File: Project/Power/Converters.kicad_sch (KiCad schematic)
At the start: 36 parts, among them J16 5V_2A, J17 5V_6A, U15 TPS560200, U16 MIC5219-3.3YM5, U17 TPS562200, U18 TPS54627

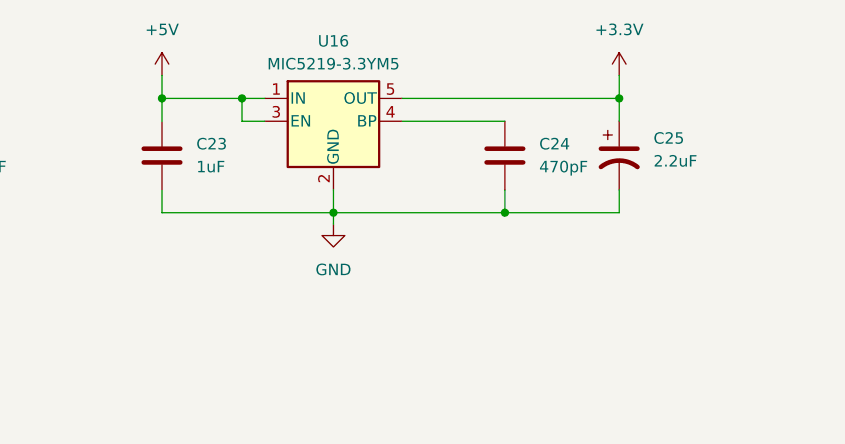
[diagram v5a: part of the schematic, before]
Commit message: Add converter and motor power routing
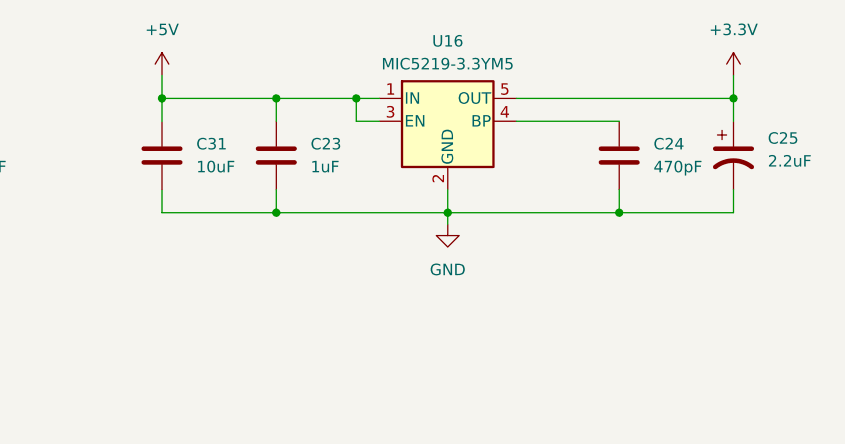
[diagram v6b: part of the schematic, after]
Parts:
- added C31: 10uF, Capacitor_SMD:C_1206_3216Metric, symbol Device:C
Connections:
- net +5V: now also C31.1
- net GND: now also C31.2
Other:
- moved on the sheet: C23, C24, C25, U16
